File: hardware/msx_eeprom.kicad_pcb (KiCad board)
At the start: 2 copper layers, 102.8 x 65.4 mm, 102 parts, among them J1 Conn_02x07_Odd_Even, P1 MSX_CONNECTOR, U1 AT28C256-15PU

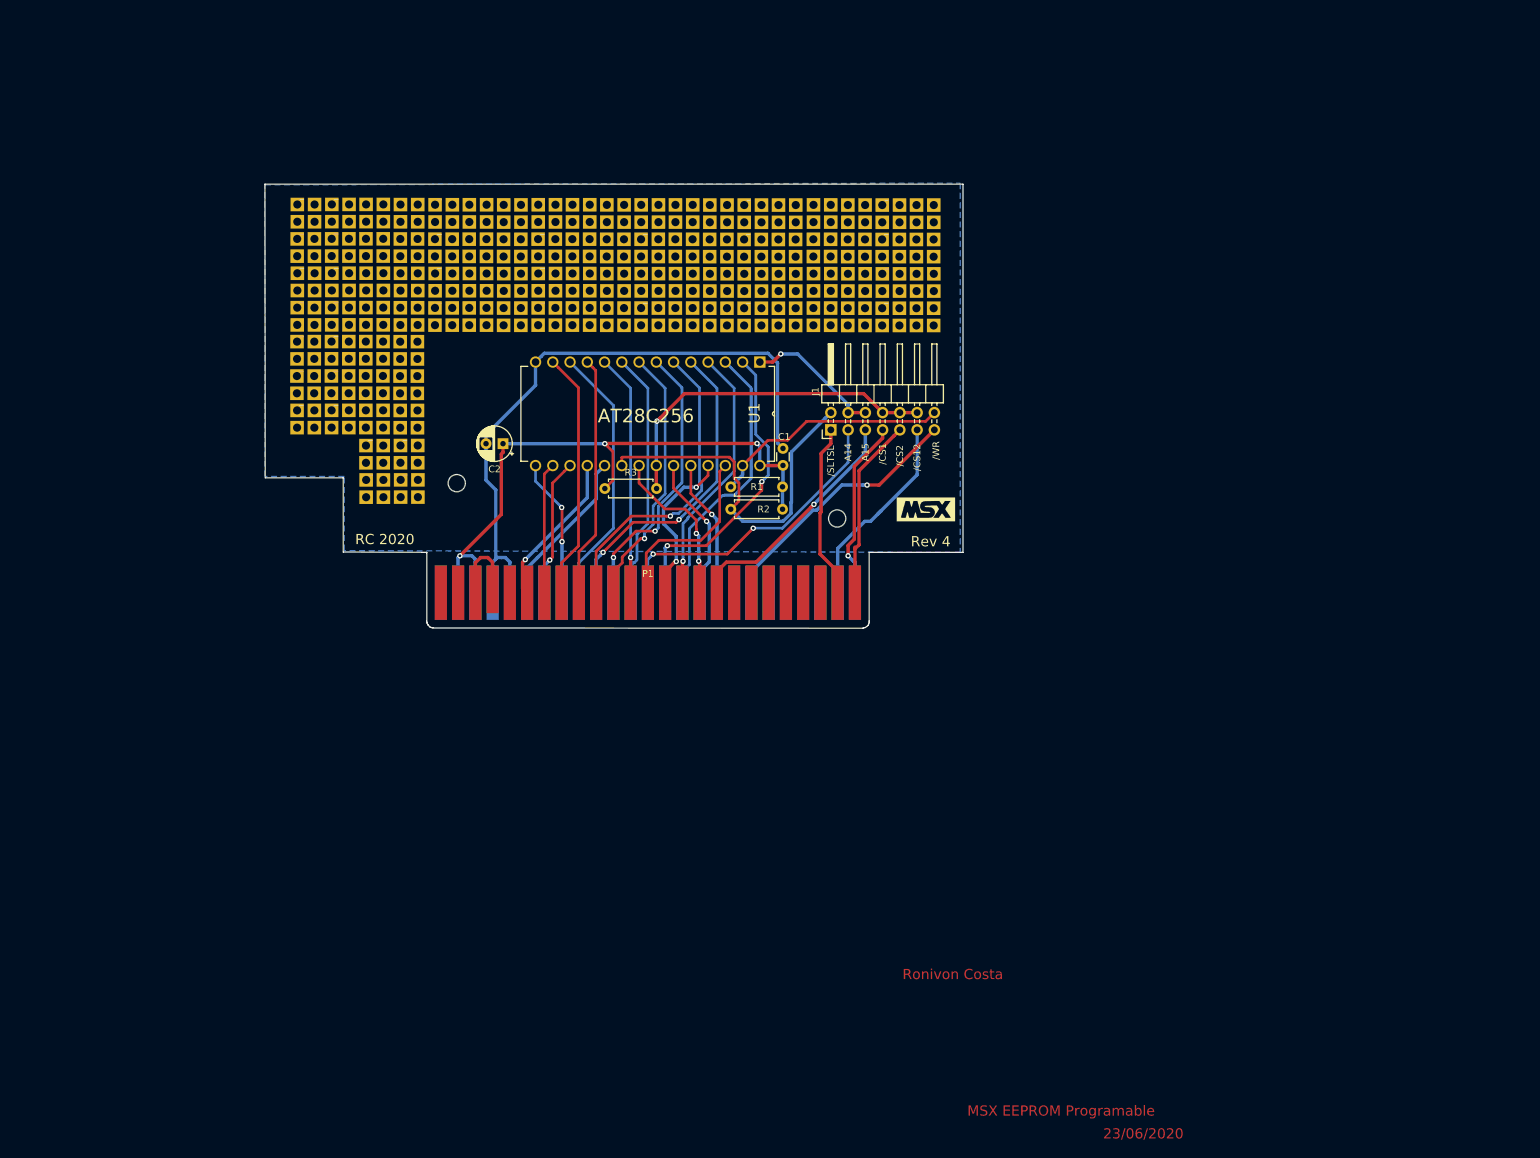
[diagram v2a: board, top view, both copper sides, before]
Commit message: Updated pcb to rev 5 - moved jumpers to better position
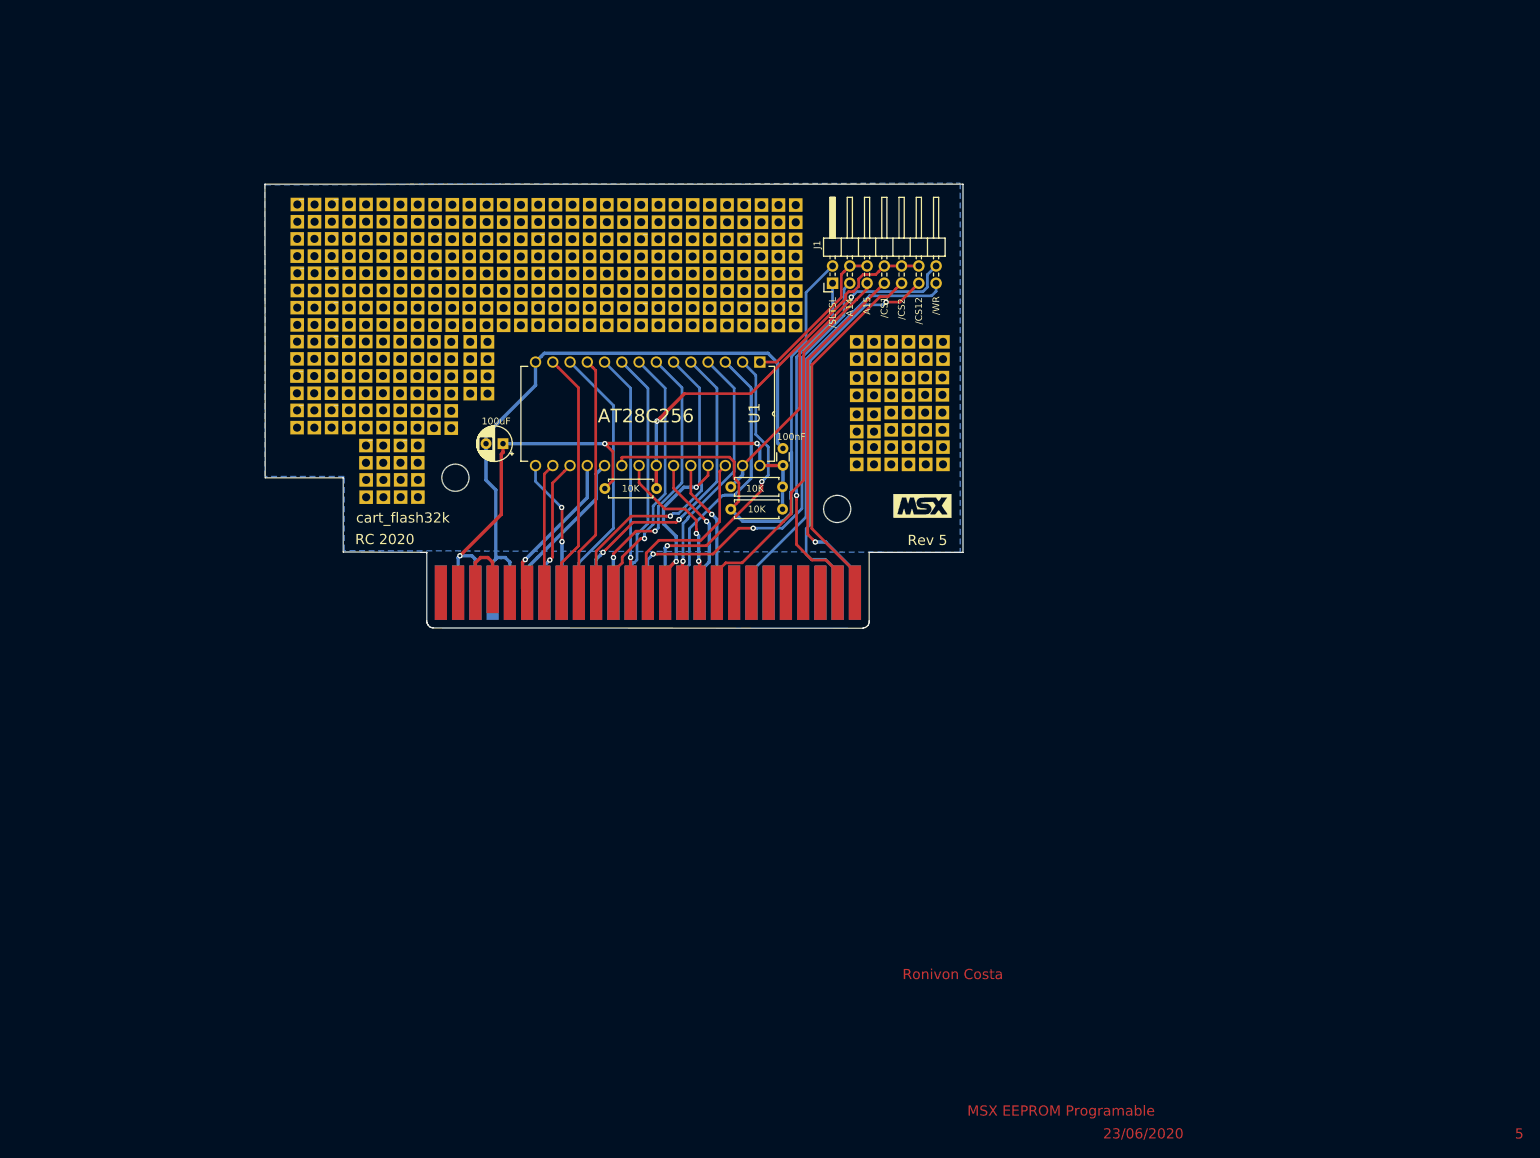
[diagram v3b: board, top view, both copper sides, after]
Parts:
- removed the _ at (170.9, 71.5)
- removed the _ at (165.9, 66.4)
- removed the _ at (181.0, 66.4)
- removed the _ at (176.0, 61.4)
- removed the _ at (170.9, 61.4)
- removed the _ at (181.0, 61.4)
- removed the _ at (176.0, 56.3)
- removed the _ at (165.8, 61.4)
- removed the _ at (170.9, 66.4)
- removed the _ at (176.0, 71.5)
- removed the _ at (181.0, 71.5)
- removed the _ at (170.9, 56.3)
- removed the _ at (165.8, 56.3)
- removed the _ at (181.0, 56.3)
- removed the _ at (165.8, 71.5)
- removed the _ at (176.0, 66.4)
- added _: _, Connector_Wire:SolderWirePad_2x02_P2.54mm_Drill0.8mm, F.Cu at (110.0, 86.6)
- added _: _, Connector_Wire:SolderWirePad_2x02_P2.54mm_Drill0.8mm, F.Cu at (177.3, 91.9)
- added _: _, Connector_Wire:SolderWirePad_2x02_P2.54mm_Drill0.8mm, F.Cu at (182.4, 91.9)
- added _: _, Connector_Wire:SolderWirePad_2x02_P2.54mm_Drill0.8mm, F.Cu at (177.3, 86.9)
- added _: _, Connector_Wire:SolderWirePad_2x02_P2.54mm_Drill0.8mm, F.Cu at (177.3, 81.8)
- added _: _, Connector_Wire:SolderWirePad_2x02_P2.54mm_Drill0.8mm, F.Cu at (182.3, 86.9)
- added _: _, Connector_Wire:SolderWirePad_2x02_P2.54mm_Drill0.8mm, F.Cu at (182.3, 81.7)
- added _: _, Connector_Wire:SolderWirePad_2x02_P2.54mm_Drill0.8mm, F.Cu at (177.3, 76.5)
- added _: _, Connector_Wire:SolderWirePad_2x02_P2.54mm_Drill0.8mm, F.Cu at (182.4, 76.5)
- added _: _, Connector_Wire:SolderWirePad_2x02_P2.54mm_Drill0.8mm, F.Cu at (115.3, 81.5)
- added _: _, Connector_Wire:SolderWirePad_2x02_P2.54mm_Drill0.8mm, F.Cu at (110.0, 81.5)
- added _: _, Connector_Wire:SolderWirePad_2x02_P2.54mm_Drill0.8mm, F.Cu at (115.3, 76.5)
- added _: _, Connector_Wire:SolderWirePad_2x02_P2.54mm_Drill0.8mm, F.Cu at (110.0, 76.5)
- added _: _, Connector_Wire:SolderWirePad_2x02_P2.54mm_Drill0.8mm, F.Cu at (172.2, 76.5)
- added _: _, Connector_Wire:SolderWirePad_2x02_P2.54mm_Drill0.8mm, F.Cu at (172.2, 81.8)
- added _: _, Connector_Wire:SolderWirePad_2x02_P2.54mm_Drill0.8mm, F.Cu at (172.2, 87.1)
- added _: _, Connector_Wire:SolderWirePad_2x02_P2.54mm_Drill0.8mm, F.Cu at (172.2, 91.9)
- moved J1 21.6 mm to (168.7, 67.8)
- moved G*** 0.72 mm to (181.9, 100.6)
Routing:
- net cs12: track 30.3 -> 58.3 mm, vias 0 -> 1
- net cs1: track 27.4 -> 54.9 mm
- net cs2: track 27.0 -> 54.4 mm
- net sltsl: track 28.9 -> 54.7 mm, vias 0 -> 1
- net wr: track 38.7 -> 62.2 mm, vias 1 -> 0
- net mem_ce: track 53.1 -> 74.9 mm
- net A14: track 48.2 -> 69.9 mm
- net A15: track 38.8 -> 59.3 mm, vias 1 -> 0
- net mem_we: track 35.3 -> 50.7 mm, vias 0 -> 1
- net mem_oe: track 51.7 -> 59.6 mm
- net mem_A14: track 20.3 -> 23.6 mm, vias 1 -> 0
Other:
- board text added: "5"
- board text added: "Rev 5"
- board text added: "cart_flash32k"
- board text added: "https://github.com/costarc/msxcart_flash32k"
- board text removed: "Rev 4"

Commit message: Imported in Kicad6
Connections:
- P1 pad 10: Net-(P1-Pad10) -> unconnected-(P1-Pad10)
- P1 pad 11: Net-(P1-Pad11) -> unconnected-(P1-Pad11)
- P1 pad 12: Net-(P1-Pad12) -> unconnected-(P1-Pad12)
- P1 pad 15: Net-(P1-Pad15) -> unconnected-(P1-Pad15)
- P1 pad 16: Net-(P1-Pad16) -> unconnected-(P1-Pad16)
- P1 pad 42: Net-(P1-Pad42) -> unconnected-(P1-Pad42)
- P1 pad 48: Net-(P1-Pad48) -> unconnected-(P1-Pad48)
- P1 pad 49: Net-(P1-Pad49) -> unconnected-(P1-Pad49)
- P1 pad 5: Net-(P1-Pad5) -> unconnected-(P1-Pad5)
- P1 pad 50: Net-(P1-Pad50) -> unconnected-(P1-Pad50)
- P1 pad 6: Net-(P1-Pad6) -> unconnected-(P1-Pad6)
- P1 pad 7: Net-(P1-Pad7) -> unconnected-(P1-Pad7)
- P1 pad 8: Net-(P1-Pad8) -> unconnected-(P1-Pad8)
- P1 pad 9: Net-(P1-Pad9) -> unconnected-(P1-Pad9)
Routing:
- net A13: track 27.3 -> 30.7 mm
- net A14: track 69.9 -> 66.8 mm
- net Net-(P1-Pad44): track 11.5 -> 13.5 mm
- net mem_oe: track 59.6 -> 58.9 mm
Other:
- net class Default removed
- board text added: "RC 2023"
- board text added: "Rev 6"
- board text removed: "RC 2020"
- board text removed: "Rev 5"

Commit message: Rev 7
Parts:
- removed R2, R3: 10K, Resistor_THT:R_Axial_DIN0207_L6.3mm_D2.5mm_P7.62mm_Horizontal
- removed the _ at (100.0, 56.2)
- removed the _ at (140.5, 56.3)
- removed the _ at (115.2, 56.3)
- removed the _ at (89.9, 56.2)
- removed the _ at (94.9, 56.2)
- removed the _ at (110.1, 56.3)
- removed the _ at (135.4, 56.3)
- removed the _ at (120.2, 56.3)
- removed the _ at (125.3, 56.3)
- removed the _ at (130.4, 56.3)
- removed the _ at (105.0, 56.2)
- removed the _ at (150.6, 56.3)
- removed the _ at (145.5, 56.3)
- removed the _ at (155.7, 56.3)
- removed the _ at (160.7, 56.3)
- removed the _ at (182.4, 91.9)
- removed the _ at (182.3, 81.7)
- removed the _ at (182.4, 76.5)
- removed the _ at (182.3, 86.9)
- added _: _, Connector_Wire:SolderWirePad_2x02_P2.54mm_Drill0.8mm, F.Cu at (102.4, 46.0)
- added _: _, Connector_Wire:SolderWirePad_2x02_P2.54mm_Drill0.8mm, F.Cu at (92.2, 46.0)
- added _: _, Connector_Wire:SolderWirePad_2x02_P2.54mm_Drill0.8mm, F.Cu at (97.3, 46.0)
- added _: _, Connector_Wire:SolderWirePad_2x02_P2.54mm_Drill0.8mm, F.Cu at (127.6, 30.8)
- added _: _, Connector_Wire:SolderWirePad_2x02_P2.54mm_Drill0.8mm, F.Cu at (51.7, 61.2)
- added _: _, Connector_Wire:SolderWirePad_2x02_P2.54mm_Drill0.8mm, F.Cu at (71.9, 61.3)
- added _: _, Connector_Wire:SolderWirePad_2x02_P2.54mm_Drill0.8mm, F.Cu at (127.6, 35.9)
- added _: _, Connector_Wire:SolderWirePad_2x02_P2.54mm_Drill0.8mm, F.Cu at (77.2, 56.1)
- added _: _, Connector_Wire:SolderWirePad_2x02_P2.54mm_Drill0.8mm, F.Cu at (117.5, 46.0)
- added _: _, Connector_Wire:SolderWirePad_2x02_P2.54mm_Drill0.8mm, F.Cu at (87.2, 46.0)
- added _: _, Connector_Wire:SolderWirePad_2x02_P2.54mm_Drill0.8mm, F.Cu at (107.4, 46.0)
- added _: _, Connector_Wire:SolderWirePad_2x02_P2.54mm_Drill0.8mm, F.Cu at (112.5, 46.0)
- added _: _, Connector_Wire:SolderWirePad_2x02_P2.54mm_Drill0.8mm, F.Cu at (82.1, 46.0)
- added _: _, Connector_Wire:SolderWirePad_2x02_P2.54mm_Drill0.8mm, F.Cu at (56.8, 61.2)
- J1: footprint Connector_PinHeader_2.54mm:PinHeader_2x07_P2.54mm_Horizontal -> Connector_PinHeader_2.54mm:PinHeader_2x03_P2.54mm_Horizontal
- P1: footprint MyFootprints:card_edge_connector -> Roni Footprints:MSX_CART_SW_Official
- moved P1 68.7 mm to (97.1, 56.8)
- moved _ 48.9 mm to (112.4, 30.8)
- moved _ 48.9 mm to (51.7, 35.7)
- moved _ 48.9 mm to (112.5, 35.8)
- moved _ 48.9 mm to (117.5, 40.9)
- moved _ 48.9 mm to (92.2, 30.7)
- moved _ 48.9 mm to (87.2, 35.8)
- moved _ 48.9 mm to (61.8, 30.7)
- moved _ 48.9 mm to (72.0, 35.8)
- moved _ 48.9 mm to (87.2, 30.7)
- moved _ 48.9 mm to (51.7, 30.7)
- moved _ 48.9 mm to (66.9, 35.8)
- moved _ 48.9 mm to (56.8, 35.7)
- moved _ 48.9 mm to (92.3, 35.8)
- moved _ 48.9 mm to (102.3, 40.9)
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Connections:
- R1 pad 2: mem_we -> mem_ce
- U1 pad 22: mem_oe -> cs12
- U1 pad 27: mem_we -> wr
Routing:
- net mem_oe: track 58.9 -> 0.00 mm, vias 1 -> 0
- net cs1: track 54.9 -> 0.00 mm, vias 1 -> 0
- net cs2: track 54.4 -> 0.00 mm
- net mem_we: track 50.7 -> 0.00 mm, vias 1 -> 0
- net wr: track 62.2 -> 28.1 mm, vias 0 -> 1
- net A7: track 64.7 -> 42.0 mm
- net cs12: track 58.3 -> 37.4 mm
- net mem_ce: track 74.9 -> 61.5 mm
- net +5V: track 90.1 -> 77.5 mm
- net mem_A14: track 23.6 -> 30.2 mm
- net A14: track 66.8 -> 70.9 mm
- net A15: track 59.3 -> 61.6 mm
- net A13: track 30.7 -> 32.7 mm
- net sltsl: track 54.7 -> 56.6 mm
- net Net-(P1-Pad44): track 13.5 -> 11.6 mm
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- removed copper zone on B.Cu, net GNDREF
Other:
- board size 102.8 x 65.4 mm -> 99.8 x 64 mm
- board text added: "Rev 7"
- board text added: "_"
- board text removed: "/CS1"
- board text removed: "/CS12"
- board text removed: "/CS2"
- board text removed: "/WR"
- board text removed: "23/06/2020"
- board text removed: "5"
- board text removed: "MSX EEPROM Programable"
- board text removed: "RC 2023"
- board text removed: "Rev 6"
- board text removed: "Ronivon Costa"
